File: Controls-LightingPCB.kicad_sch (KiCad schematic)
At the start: 70 parts, among them J1 MinionConn, J2 12VPWRCONN, SW5 TURN_SIGNAL_SW

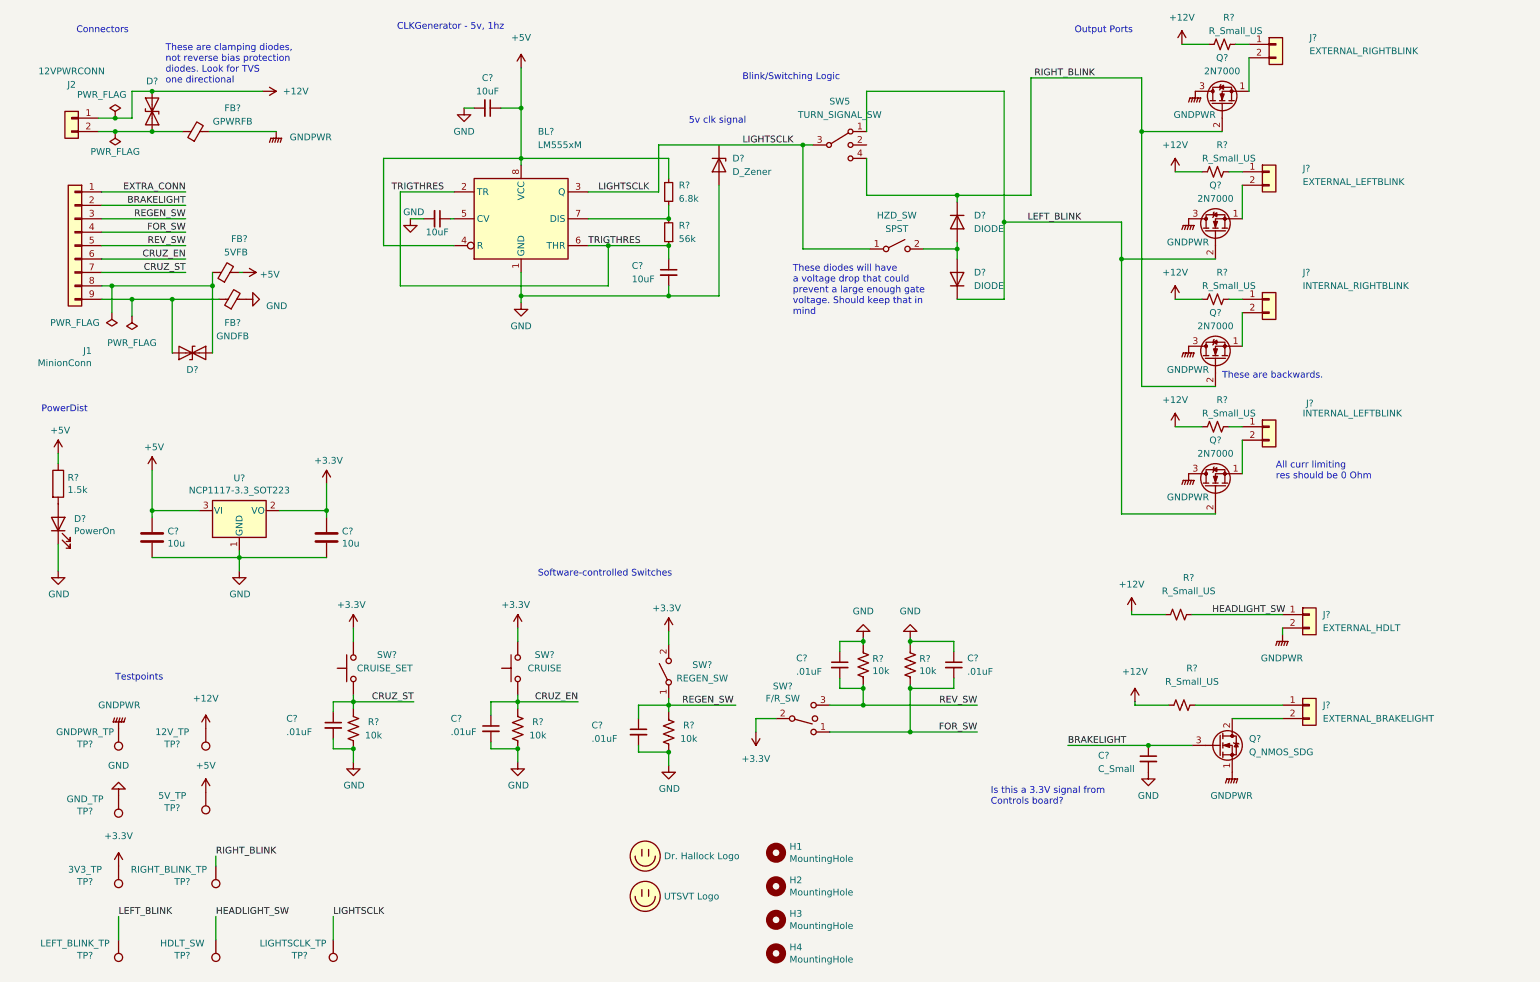
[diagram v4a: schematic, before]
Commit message: added pull-downs for mosfets, fixed mosfet orientation, added real diodes
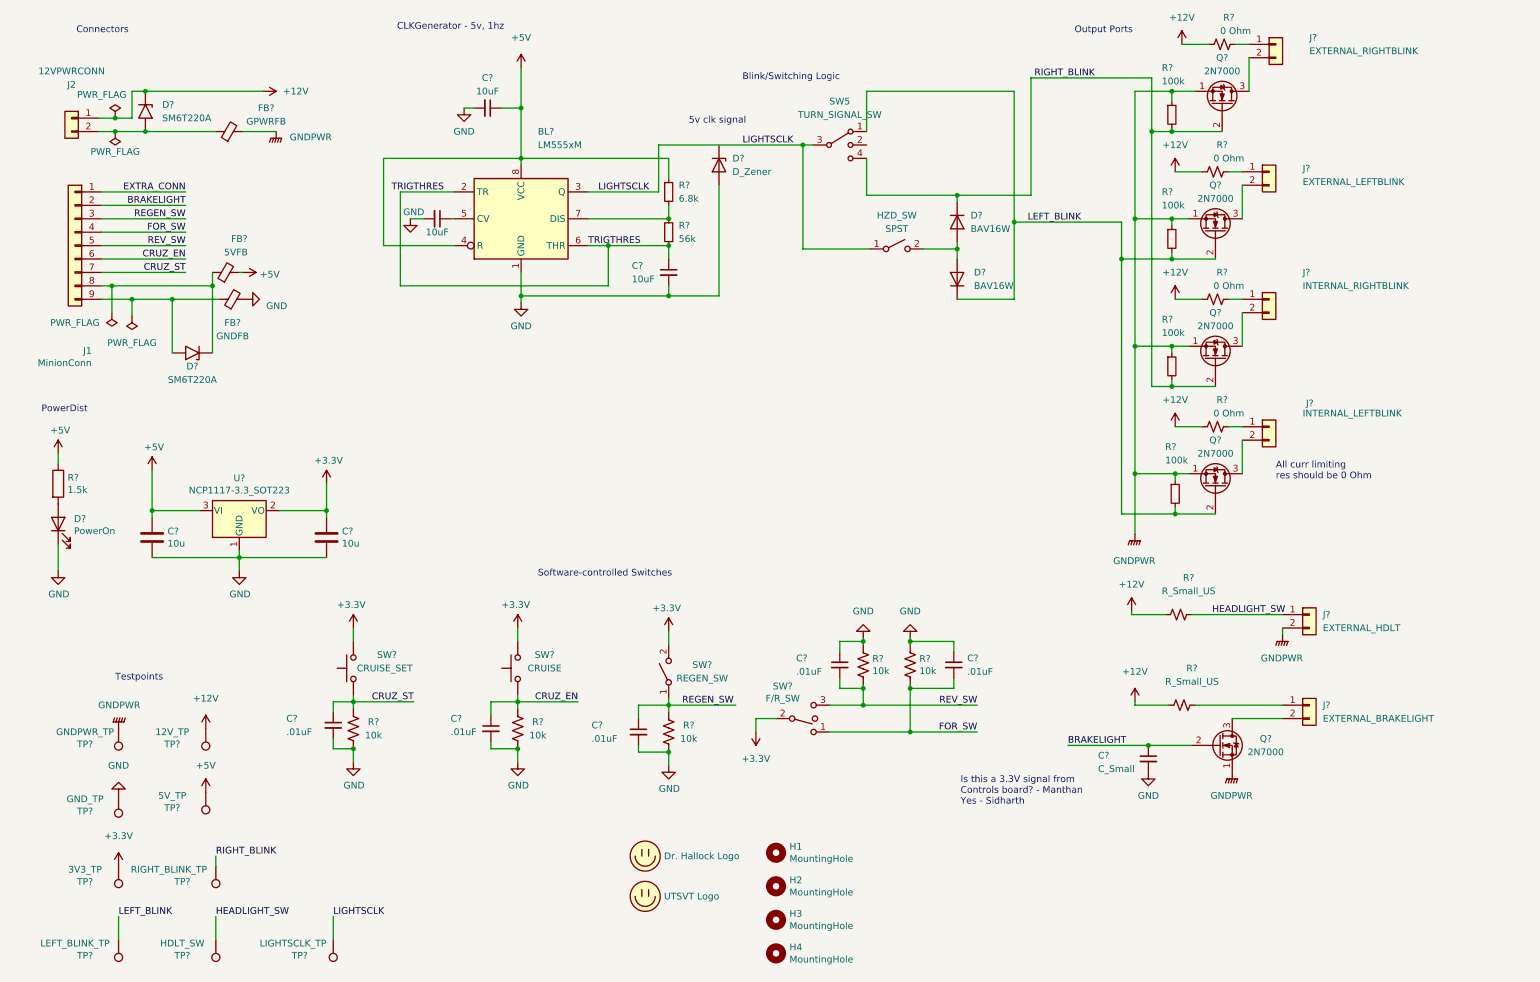
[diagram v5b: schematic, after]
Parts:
- removed D? (x2): SD05_SOD323, Diode_SMD:D_SOD-323, symbol Diode:SD05_SOD323
- removed D? (x2): DIODE, symbol Simulation_SPICE:DIODE
- removed Q?: Q_NMOS_SDG, symbol Device:Q_NMOS_SDG
- added D? (x2): BAV16W, Diode_SMD:D_SOD-123, symbol Diode:BAV16W
- added D? (x2): SM6T220A, Diode_SMD:D_SMB, symbol Diode:SM6T220A
- added Q?: 2N7000, Package_TO_SOT_THT:TO-92_Inline, symbol Transistor_FET:2N7000
- added R? (x4): 100k, symbol Device:R_Small
- R? (x4): value R_Small_US -> 0 Ohm
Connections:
- net +12V: now also D?.1 (A1)
- net BRAKELIGHT: now also Q?.2 (G)
- net GNDPWR: now also Q?.1 (S), Q?.1 (S), Q?.1 (S), Q?.1 (S), Q?.1 (S), R?.1, R?.1, R?.1, R?.1; no longer Q?.3 (D), Q?.3 (D), Q?.3 (D), Q?.3 (D)
- net LEFT_BLINK: now also D?.1 (K), R?.2, R?.2
- net RIGHT_BLINK: now also D?.1 (K), R?.2, R?.2
- net at FB?.1, J1.8 (Pin_8): now also D?.1 (A1)
- net at FB?.1, J1.9 (Pin_9): now also D?.2 (A2)
- net at J?.2 (Pin_2): now also Q?.3 (D)
- net at J?.2 (Pin_2): now also Q?.3 (D); no longer Q?.1 (S) (x4)
- net at FB?.1, J2.2 (Pin_2): now also D?.2 (A2)
- net at HZD_SW.2 (B): now also D?.2 (A), D?.2 (A)
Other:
- note added: "Is this a 3.3V signal from Controls board? - Manthan Yes - Sidharth"
- note removed: "Is this a 3.3V signal from Controls board?"
- note removed: "These are backwards."
- note removed: "These are clamping diodes, not reverse bias protection diodes. Look for TVS one directional"
- note removed: "These diodes will have a voltage drop that could prevent a large enough gate voltage. Should keep that in mind"
- moved on the sheet: FB?, Q?

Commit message: Added a few questions and comments for design review
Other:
- note added: "Also might be a Manthan question but do you need diodes for the individual right and left blink control signals (the part only connected to the the turn signal switch? I don't think you do but just want to double check - Hannah"
- note added: "Is this the same switch you'll be using for the turn signal switch SW5? (ie middle is floating) If it is, I would use the same symbol - Hannah"
- note added: "Might need to be a question for Manthan but why is the ferrite bead only needed for GNDPWR and not +12V? - Hannah"
- note added: "Resistance values for these curr limiting resistors will be calculated in the future when the LEDs are selected"
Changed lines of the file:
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@@
     (stroke (width 0) (type default) (color 0 0 0 0))
+  )
+  (text "Is this the same switch you'll be using for the \nturn signal switch SW5? (ie middle is floating)\nIf it is, I would use the same symbol\n- Hannah"
+    (at 138.43 165.1 0)
+    (effects (font (size 1.27 1.27)) (justify left bottom))
+  )
+  (text "Resistance values for these curr limiting resistors  \nwill be calculated in the future when the LEDs are selected"
+    (at 226.06 113.03 0)
+    (effects (font (size 1.27 1.27)) (justify left bottom))
   )
   (text "PowerDist\n" (at 15.24 88.9 0)
@@
     (effects (font (size 1.27 1.27)) (justify left bottom))
   )
+  (text "Also might be a Manthan question but do you \nneed diodes for the individual right and left blink \ncontrol signals (the part only connected to the the\nturn signal switch? I don't think you do but \njust want to double check\n- Hannah"
+    (at 161.29 81.28 0)
+    (effects (font (size 1.27 1.27)) (justify left bottom))
+  )
   (text "Testpoints\n" (at 29.21 139.7 0)
     (effects (font (size 1.27 1.27)) (justify left bottom))
@@
     (effects (font (size 1.27 1.27)) (justify left bottom))
   )
+  (text "Might need to be a question for Manthan \nbut why is the ferrite bead only needed \nfor GNDPWR and not +12V?\n- Hannah"
+    (at 39.37 25.4 0)
+    (effects (font (size 1.27 1.27)) (justify left bottom))
+  )

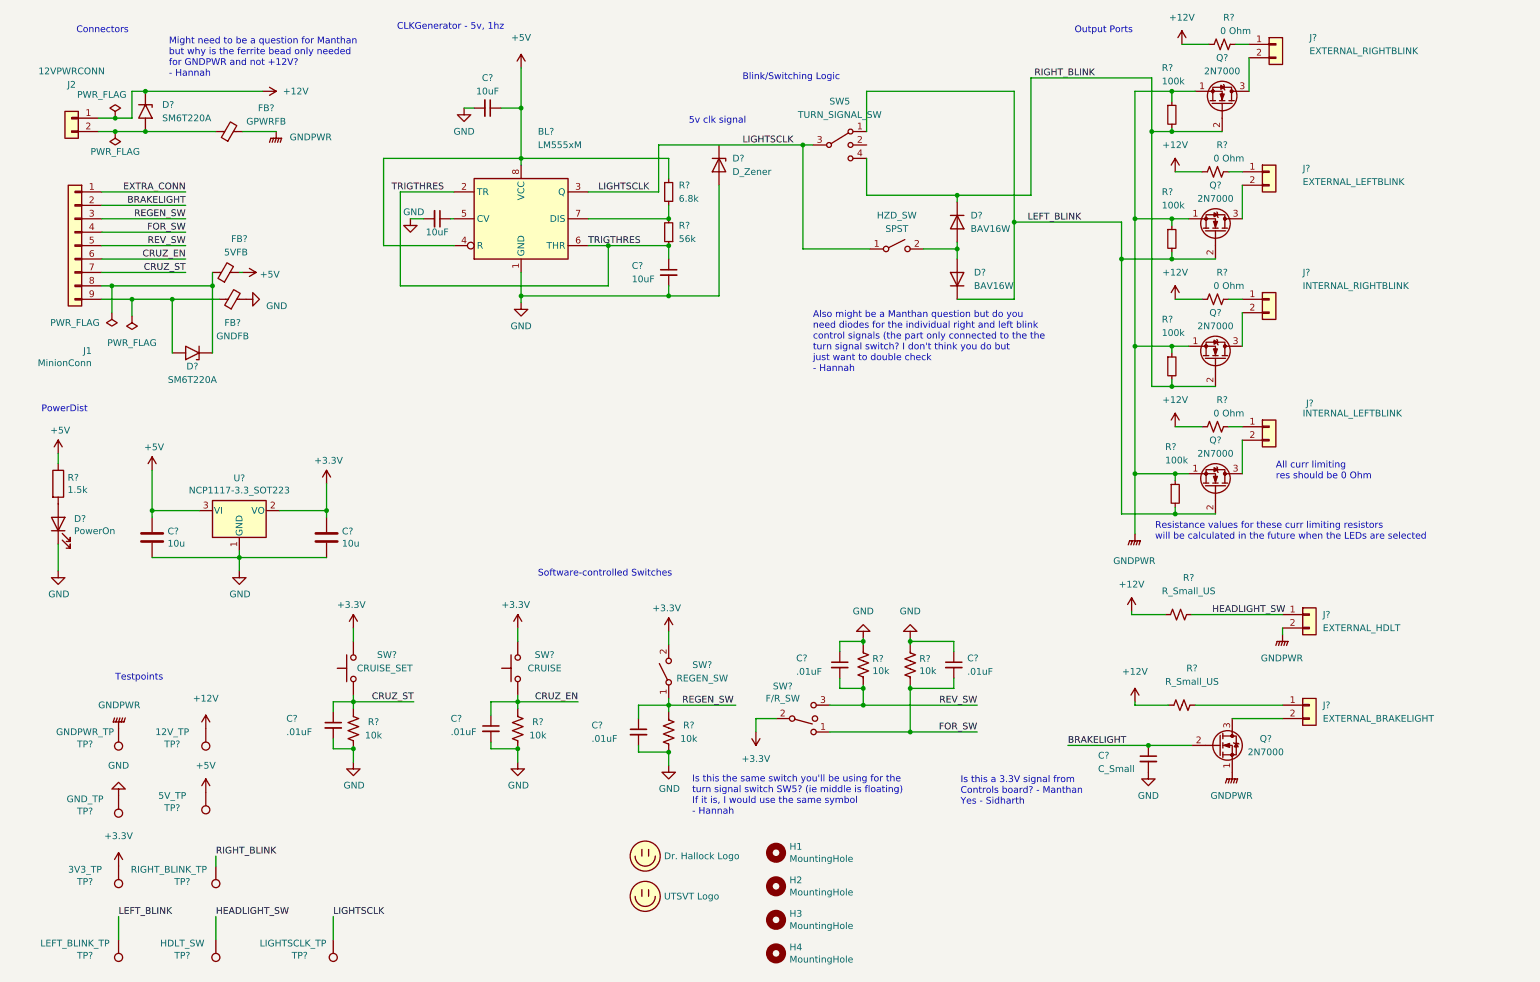
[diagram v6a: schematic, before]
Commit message: fixed diode protection
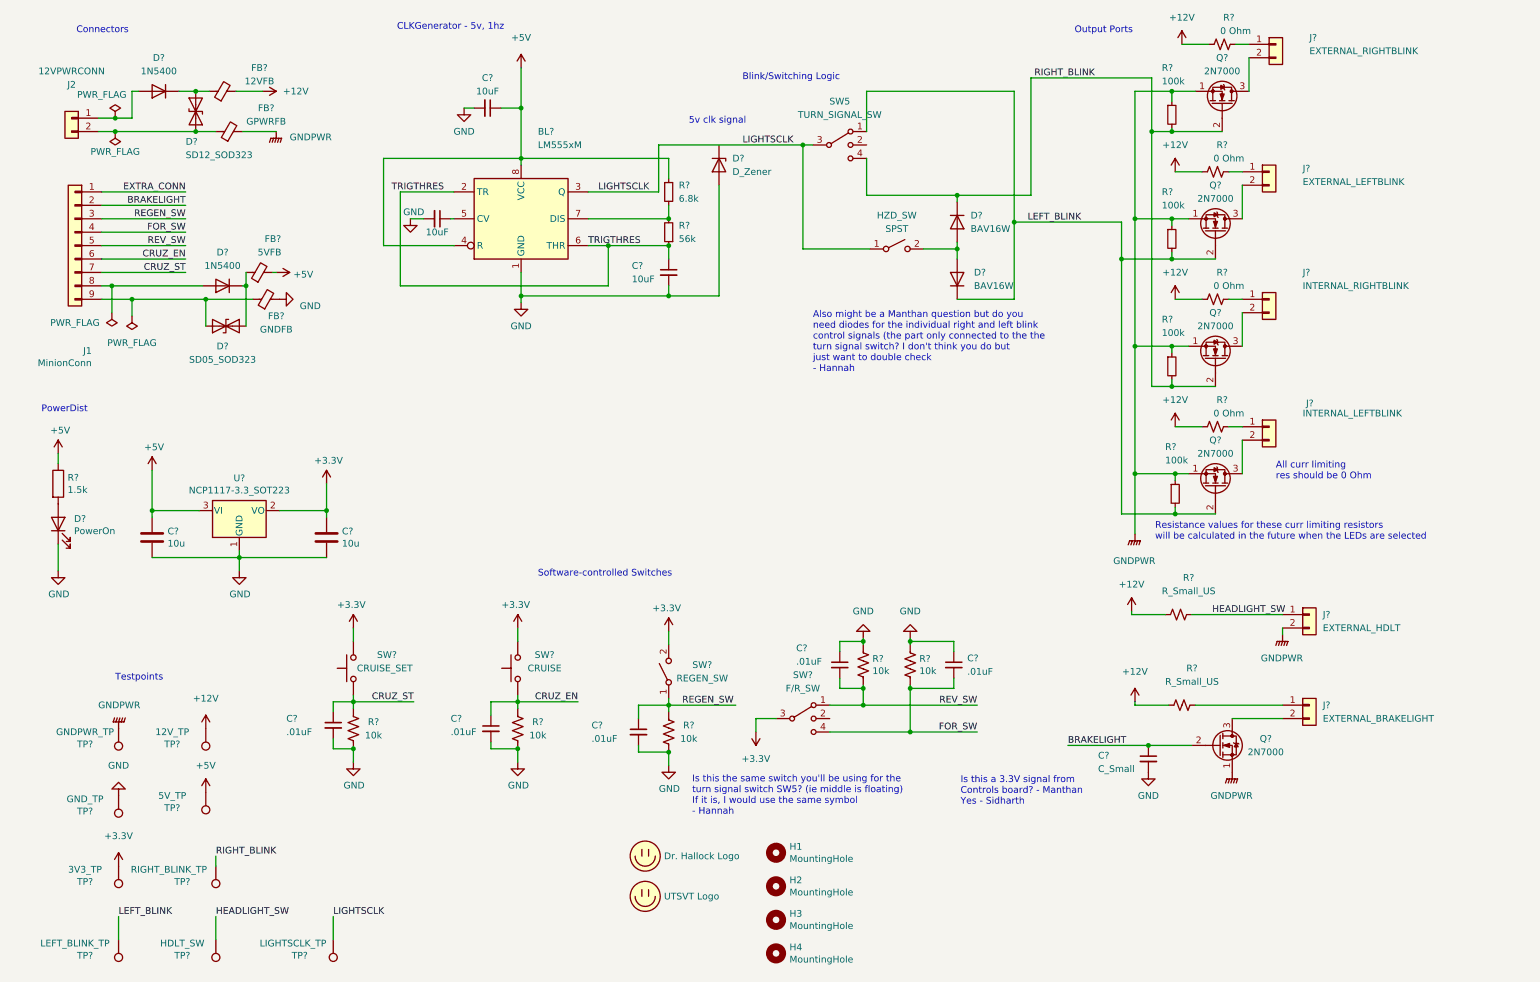
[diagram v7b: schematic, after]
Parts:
- removed D? (x2): SM6T220A, Diode_SMD:D_SMB, symbol Diode:SM6T220A
- removed SW?: F/R_SW, Connector_Molex:Molex_Micro-Fit_3.0_43650-0300_1x03_P3.00mm_Horizontal, symbol Switch:SW_SPDT_MSM
- added D? (x2): 1N5400, Diode_THT:D_DO-201AD_P15.24mm_Horizontal, symbol Diode:1N5400
- added D?: SD12_SOD323, Diode_SMD:D_SOD-323, symbol Diode:SD12_SOD323
- added D?: SD05_SOD323, Diode_SMD:D_SOD-323, symbol Diode:SD05_SOD323
- added FB?: 12VFB, symbol Device:FerriteBead_Small
- added SW?: F/R_SW, symbol Switch:SW_SP3T
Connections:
- net +12V: now also FB?.2; no longer J2.1 (Pin_1)
- net +3V3: now also SW?.3
- net FOR_SW: now also SW?.4
- net REV_SW: now also SW?.1
- net at J1.8 (Pin_8): now also D?.2 (A); no longer FB?.1
- net at FB?.1, J1.9 (Pin_9): now also D?.1 (A1)
- net at FB?.1, J2.2 (Pin_2): now also D?.1 (A1)
- new net: D?.1 (K), D?.2 (A2), FB?.1 (x2)
- new net: D?.2 (A), J2.1 (Pin_1)
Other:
- note removed: "Might need to be a question for Manthan but why is the ferrite bead only needed for GNDPWR and not +12V? - Hannah"
- moved on the sheet: FB?
